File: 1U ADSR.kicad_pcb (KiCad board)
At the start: 2 copper layers, 58.4 x 28.6 mm, 32 parts, among them J1 Gate, J2 Out, J3 PWR, Q1 BC847, Q2 BC847, Q3 BC847, U1 NE555, U2 LM358

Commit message: Finished v0.1
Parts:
- removed J3: PWR, MojaBiblioteka:Header 1x3
- removed RV1, RV2, RV3, RV4: 1M, 4ms-footprints:POT-9MM-ALPHA
- added Attack: 1M, KraakenStuff:POT-9MM-ALPHA, B.Cu at (75.6, 37.5)
- added Decay: 1M, KraakenStuff:POT-9MM-ALPHA, B.Cu at (60.7, 37.5)
- added GND +12V -12V: PWR, Connector_PinHeader_2.54mm:PinHeader_1x03_P2.54mm_Vertical, F.Cu at (26.0, 47.5)
- added Release: 1M, KraakenStuff:POT-9MM-ALPHA, B.Cu at (31.1, 37.5)
- added Sustain: 1M, KraakenStuff:POT-9MM-ALPHA, B.Cu at (45.9, 37.5)
- C1, C2, C4, C5: footprint Capacitors_SMD:C_0603_HandSoldering -> Capacitor_SMD:C_0603_1608Metric_Pad1.05x0.95mm_HandSolder
- C3: footprint Capacitors_SMD:C_0805_HandSoldering -> Capacitor_SMD:C_0603_1608Metric_Pad1.05x0.95mm_HandSolder
- D1, D2, D3, D4, D5: footprint Diodes_SMD:D_0603 -> Diode_SMD:D_0603_1608Metric_Pad1.05x0.95mm_HandSolder
- J1, J2: footprint 4ms-footprints:PJ301M-12 -> KraakenStuff:PJ301M-12
- Q1, Q2, Q3: footprint MojaBiblioteka:SOT23-BCE -> Package_TO_SOT_SMD:SOT-23
- R1, R10, R2, R3, R4, R5, R6, R7, R8, R9: footprint Resistors_SMD:R_0603_HandSoldering -> Resistor_SMD:R_0603_1608Metric_Pad1.05x0.95mm_HandSolder
- U1, U2: footprint 4ms-footprints:SOIC-8_3.9x4.9mm_Pitch1.27mm -> Package_SO:SOIC-8_3.9x4.9mm_P1.27mm
- turned Q3 to 180 degrees
- turned Q1 to 180 degrees
- turned Q2 to 180 degrees
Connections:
- R1 pad 2: Net-(J1-Pad3) -> Net-(J1-PadT)
- U2 pad 6: Net-(J2-Pad3) -> Net-(J2-PadT)
- U2 pad 7: Net-(J2-Pad3) -> Net-(J2-PadT)
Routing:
- net Net-(J2-PadT): track 0.00 -> 14.1 mm
- net Net-(J2-Pad3): track 14.1 -> 0.00 mm
- net Net-(J1-PadT): track 0.00 -> 3.77 mm
- net Net-(J1-Pad3): track 3.77 -> 0.00 mm
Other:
- board text added: "ADSR v0.1"
- board text added: "KraakenStuff"

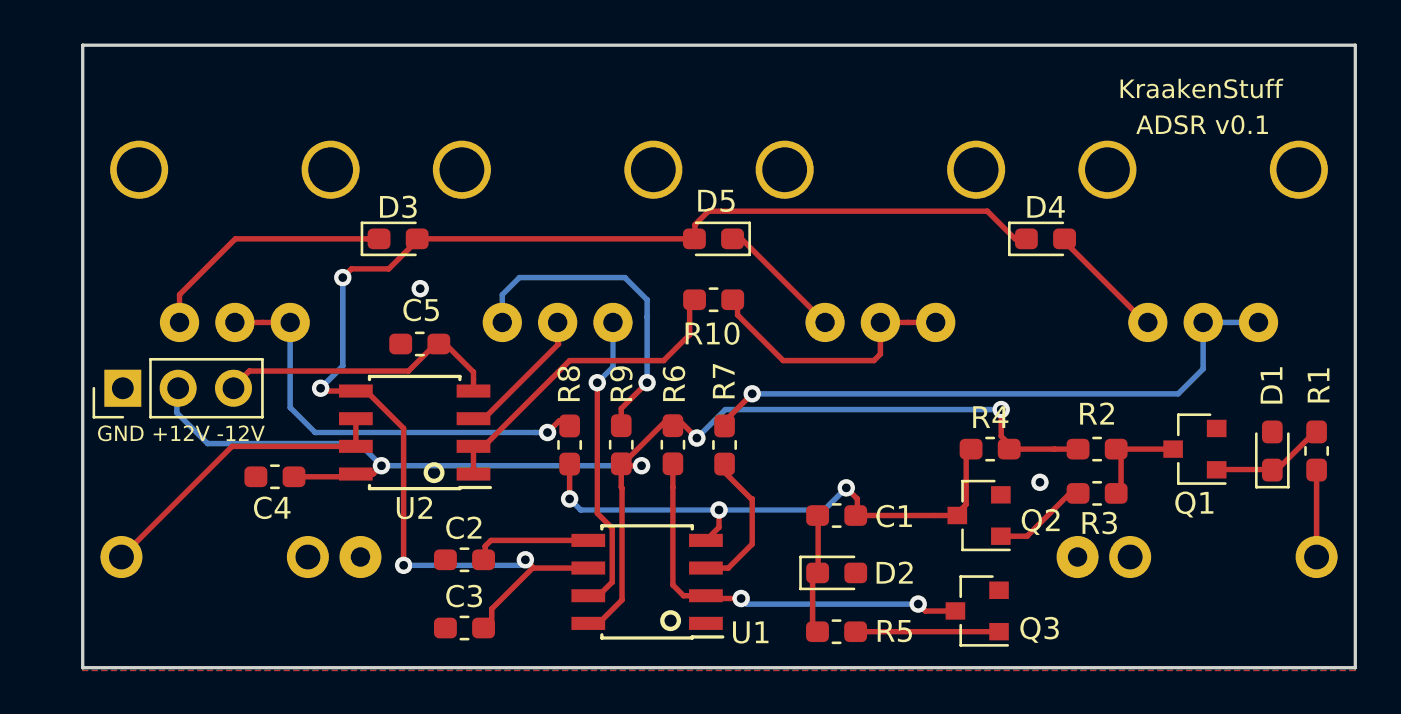
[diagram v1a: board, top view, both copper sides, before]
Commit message: Fixed potentiometers orientation.
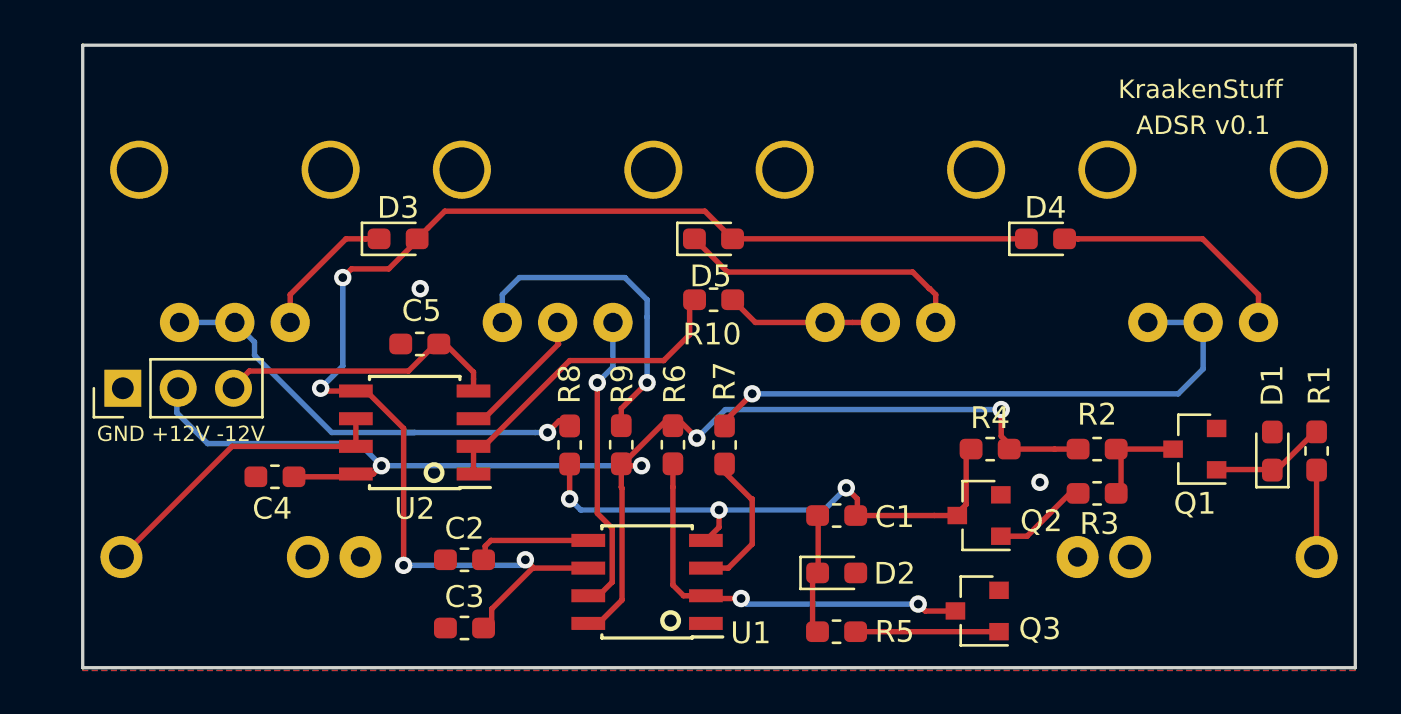
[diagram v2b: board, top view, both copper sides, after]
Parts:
- removed Attack, Decay, Release, Sustain: 1M, KraakenStuff:POT-9MM-ALPHA
- added RV1: 1M, KraakenStuff:POT-9MM-ALPHA, B.Cu at (75.6, 37.5)
- added RV2: 1M, KraakenStuff:POT-9MM-ALPHA, B.Cu at (60.7, 37.5)
- added RV3: 1M, KraakenStuff:POT-9MM-ALPHA, B.Cu at (45.9, 37.5)
- added RV4: 1M, KraakenStuff:POT-9MM-ALPHA, B.Cu at (31.1, 37.5)
- turned D5 to 0 degrees
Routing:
- net Net-(D5-Pad1): track 5.86 -> 13.4 mm
- net Net-(D4-Pad2): track 5.50 -> 11.2 mm
- net Net-(D3-Pad1): track 11.5 -> 6.41 mm
- net Net-(R10-Pad2): track 12.2 -> 7.21 mm
- net Net-(R8-Pad1): track 20.0 -> 21.1 mm
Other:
- board text added: "ATTACK"
- board text added: "DECAY"
- board text added: "RELEASE"
- board text added: "SUSTAIN"

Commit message: Changed the version on pcb
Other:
- board text added: "ADSR v0.1.1"
- board text removed: "ADSR v0.1"
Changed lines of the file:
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@@
       (outputformat 1)
       (mirror false)
-      (drillshape 1)
+      (drillshape 0)
       (scaleselection 1)
-      (outputdirectory ""))
+      (outputdirectory "Gerbers/"))
   )
   (net 0 "")
@@
     (effects (font (size 0.75 0.75) (thickness 0.12)) (justify mirror))
   )
-  (gr_text "ADSR v0.1" (at 75.565 35.433) (layer F.SilkS)
+  (gr_text "ADSR v0.1.1" (at 75.565 35.433) (layer F.SilkS)
     (effects (font (size 0.85 0.85) (thickness 0.12)))
   )
